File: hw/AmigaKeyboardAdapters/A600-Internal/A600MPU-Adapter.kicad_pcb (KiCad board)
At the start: 2 copper layers, 33 x 29.2 mm, 9 parts, among them P1 Conn_02x03_Odd_Even, P2 Conn_01x03_Male, U1 6571R4_PLCC44_MPUKEY_REV

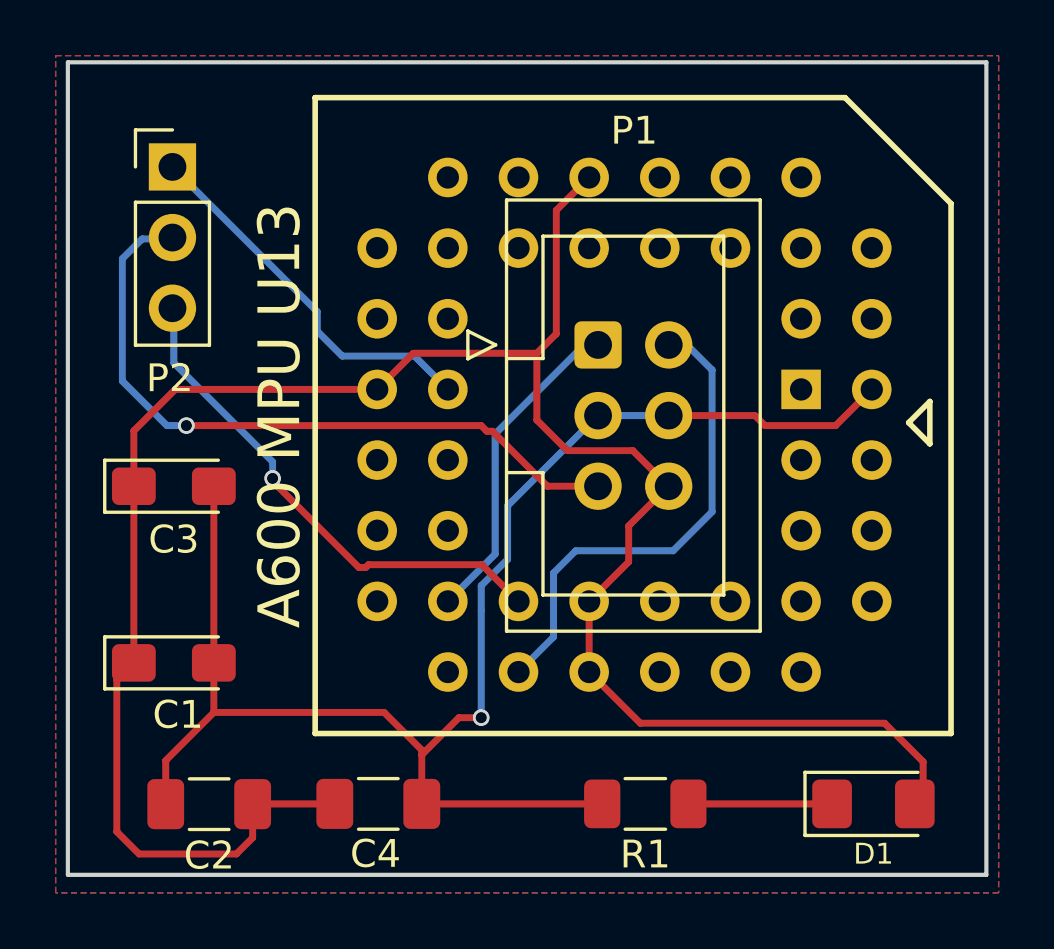
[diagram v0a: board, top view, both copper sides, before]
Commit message: Corrected F.Silkscreen for MPU U13 6570. Thanks to Pietro Colombo for pointing that issue
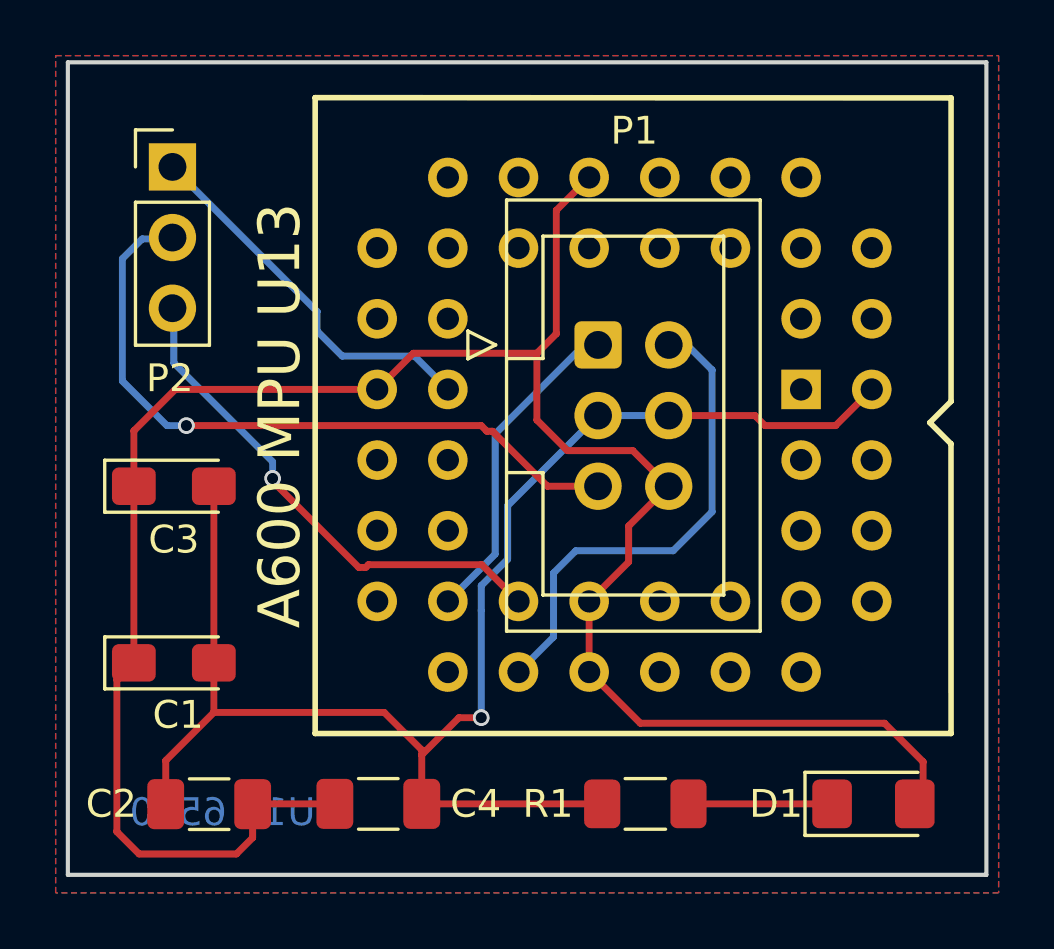
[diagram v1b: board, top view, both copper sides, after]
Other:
- board text added: "RBL007.002"
- board text added: "U13 6570"
- board text added: "designed by R.G.2018/2022/2026"
- board text removed: "RBL007.001"
- board text removed: "designed by R.G.2018/2022"

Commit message: V3 RBL007.002 With TEARDROPS - Corrected F.Silkscreen for MPU U13 6570. Thanks to Pietro Colombo for pointing that issue
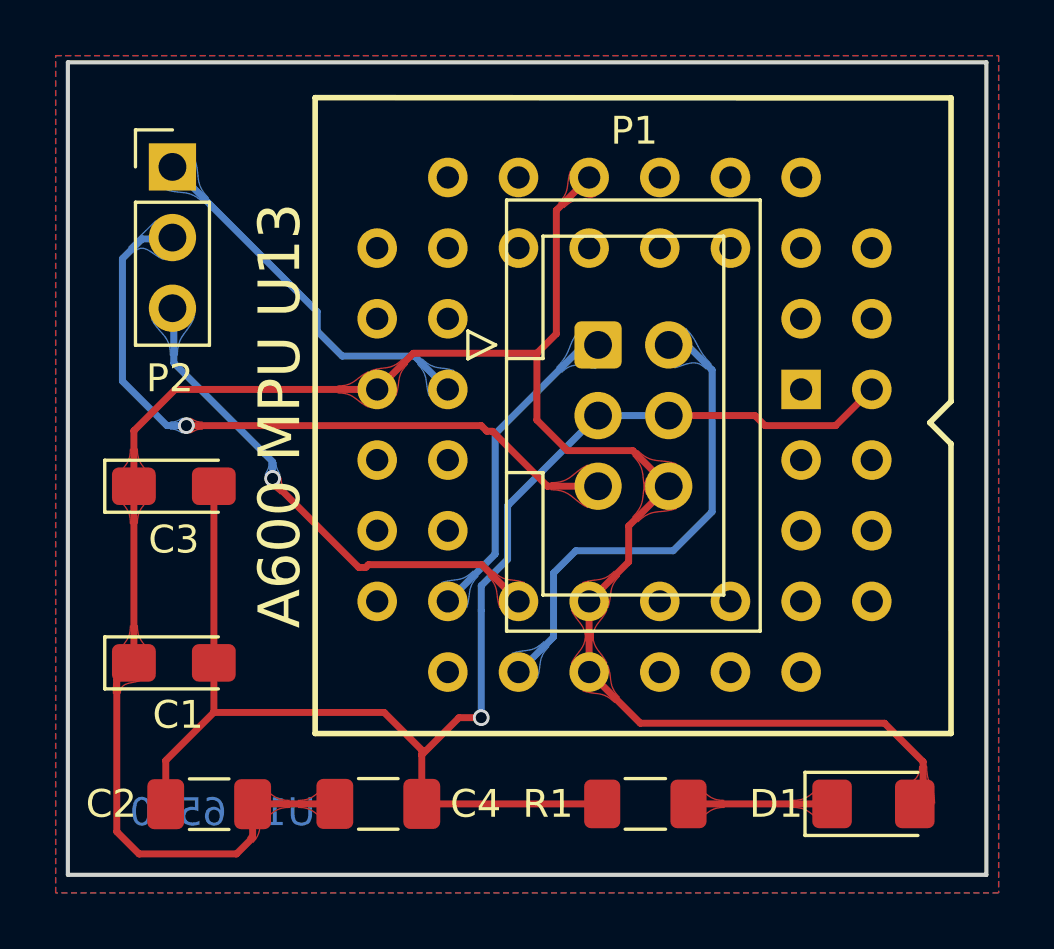
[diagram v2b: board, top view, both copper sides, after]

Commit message: Updated the symbol and the positioning of the footprint in bottom layer. Now all signals are checked with PCBEXPLORER for A600 (June Bug version) They seem to be ok. Updated from library too.
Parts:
- moved U1 9.06 mm to (161.4, 97.7), turned to 180 degrees
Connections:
- U1 pad 14: VCC -> (no net)
- U1 pad 15: KBD_DATA -> (no net)
- U1 pad 16: ~TRESET -> (no net)
- U1 pad 19: KBD_CLOCK -> (no net)
- U1 pad 22: (no net) -> VCC
- U1 pad 23: (no net) -> ~RST
- U1 pad 24: VCC -> (no net)
- U1 pad 25: ~RST -> (no net)
- U1 pad 30: (no net) -> KBD_CLOCK
- U1 pad 31: (no net) -> KBD_DATA
- U1 pad 32: (no net) -> ~TRESET
- U1 pad 33: VCC -> (no net)
- U1 pad 34: (no net) -> VCC
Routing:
- net GND: track 54.4 -> 32.9 mm, vias 1 -> 2
- net ~RST: track 13.6 -> 27.4 mm
- net VCC: track 78.0 -> 68.3 mm, vias 0 -> 1
- net KBD_RESET: track 25.2 -> 20.3 mm
- net ~TRESET: track 18.4 -> 13.9 mm
- net KBD_CLOCK: track 11.7 -> 10.9 mm
- net KBD_DATA: track 17.7 -> 18.3 mm

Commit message: The symbol 6571 had the pins counter-clockwise. Now it should be corrected as seen as http://amigapcb.org/ Thanks to Pietro Colombo
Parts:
- moved U1 0.14 mm to (161.5, 97.6)
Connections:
- U1 pad 12: (no net) -> VCC
- U1 pad 13: VCC -> (no net)
- U1 pad 14: (no net) -> ~TRESET
- U1 pad 15: (no net) -> KBD_DATA
- U1 pad 16: (no net) -> KBD_CLOCK
- U1 pad 22: VCC -> (no net)
- U1 pad 24: (no net) -> VCC
- U1 pad 30: KBD_CLOCK -> (no net)
- U1 pad 31: KBD_DATA -> (no net)
- U1 pad 32: ~TRESET -> (no net)
- U1 pad 33: (no net) -> VCC
- U1 pad 34: VCC -> (no net)
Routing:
- net ~TRESET: track 13.9 -> 45.3 mm, vias 1 -> 0
- net VCC: track 68.3 -> 79.6 mm, vias 1 -> 0
- net KBD_CLOCK: track 10.9 -> 18.7 mm
- net KBD_DATA: track 18.3 -> 13.1 mm
- net GND: track 32.9 -> 37.7 mm
- net ~RST: track 27.4 -> 29.7 mm
- net KBD_RESET: track 20.3 -> 21.2 mm, vias 1 -> 0
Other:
- board text added: "RBL007.003"
- board text removed: "RBL007.002"
